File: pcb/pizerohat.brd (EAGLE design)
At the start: 65 x 29.9 mm, 21 parts, among them J1 MF-CON-2.54mm-01x03, J2 MF-CON-2.54mm-01x06, J3 MF-CON-2.54mm-01x03, J4 MF-CON-2.54mm-01x06, J5 MF-CON-2.54mm-01x03, J6 MF-CON-2.54mm-01x03, U1 MAX14778ETP+, U2 MAX3089CSD+, U3 MF-DSC-SOT233-BSS84

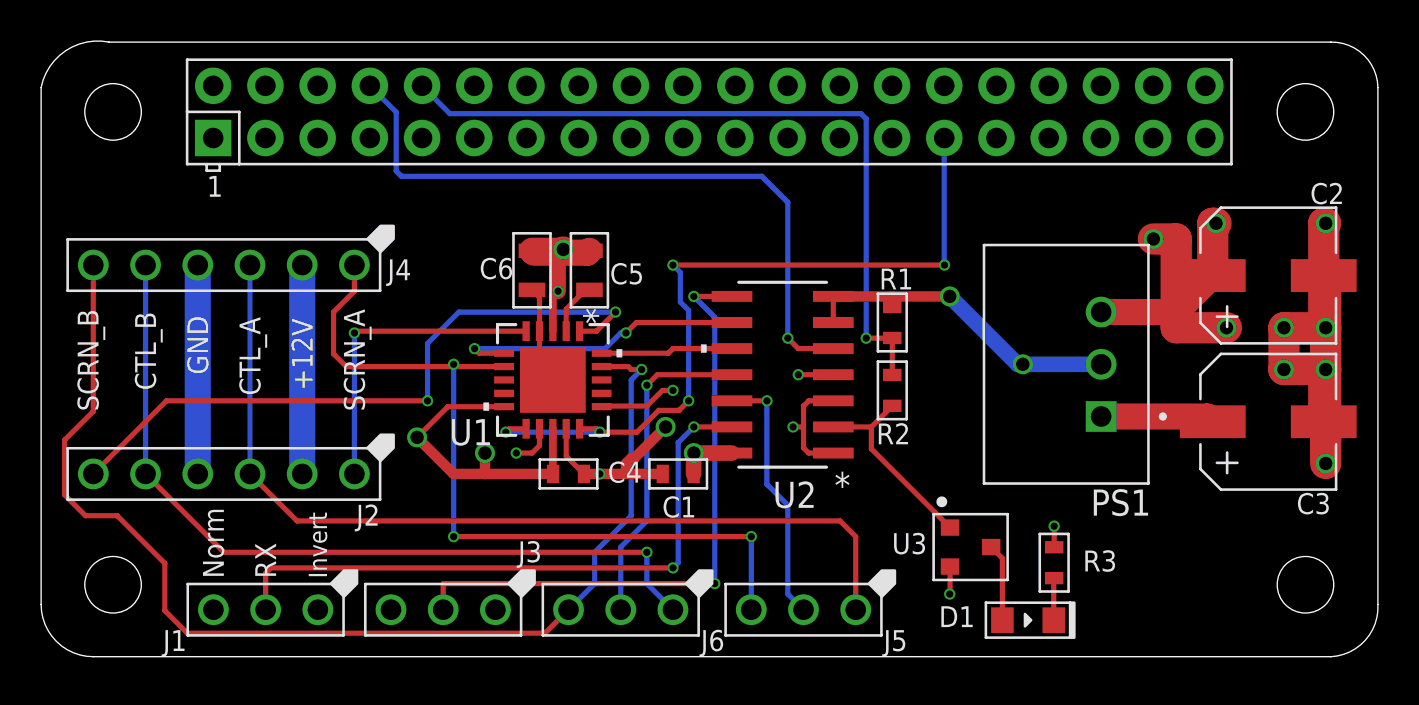
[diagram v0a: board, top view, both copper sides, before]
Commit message: Rordered mux pins, added pulldown for default muxsel
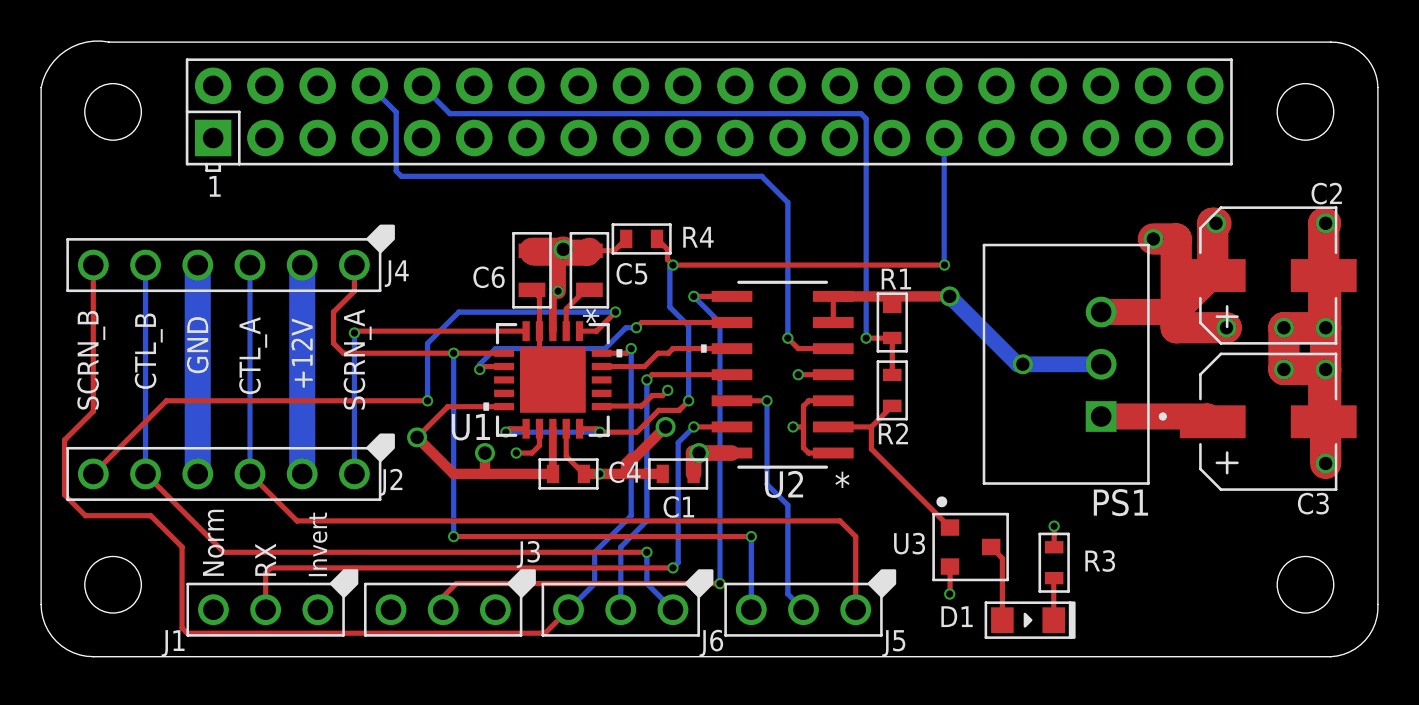
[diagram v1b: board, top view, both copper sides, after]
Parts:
- added R4: 18k, MF_Passives:R0603
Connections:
- net N$2 renamed TX_FROM_RASP
- removed net N$8: U$1.29, U1.11, U1.15
- new net MUX_SEL: R4.P$2, U$1.29, U1.11, U1.15
- net FROM_RASP_A: now also U1.7; no longer U1.6
- net FROM_RASP_B: now also U1.19; no longer U1.20
- net FROM_SCRN_A: now also U1.6; no longer U1.7
- net FROM_SCRN_B: now also U1.20; no longer U1.19
- net GND: now also R4.P$1
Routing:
- net MUX_SEL: track 0.00 -> 39.7 mm, vias 0 -> 5
- net N$8: track 37.9 -> 0.00 mm, vias 5 -> 0
- net GND: track 76.0 -> 78.0 mm
- net FROM_SCRN_B: track 56.0 -> 57.3 mm

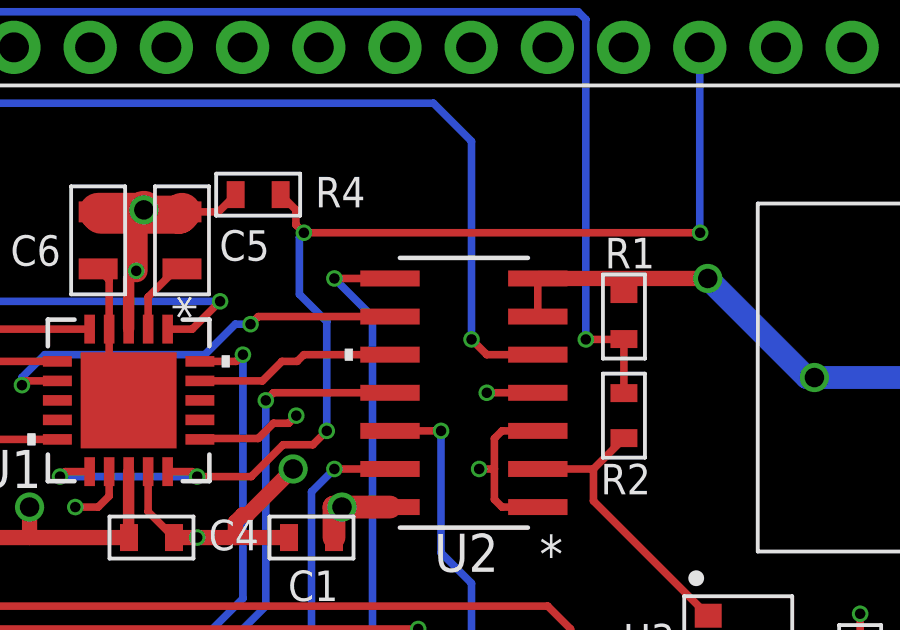
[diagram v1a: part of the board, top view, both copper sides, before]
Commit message: Power TX down when not in use
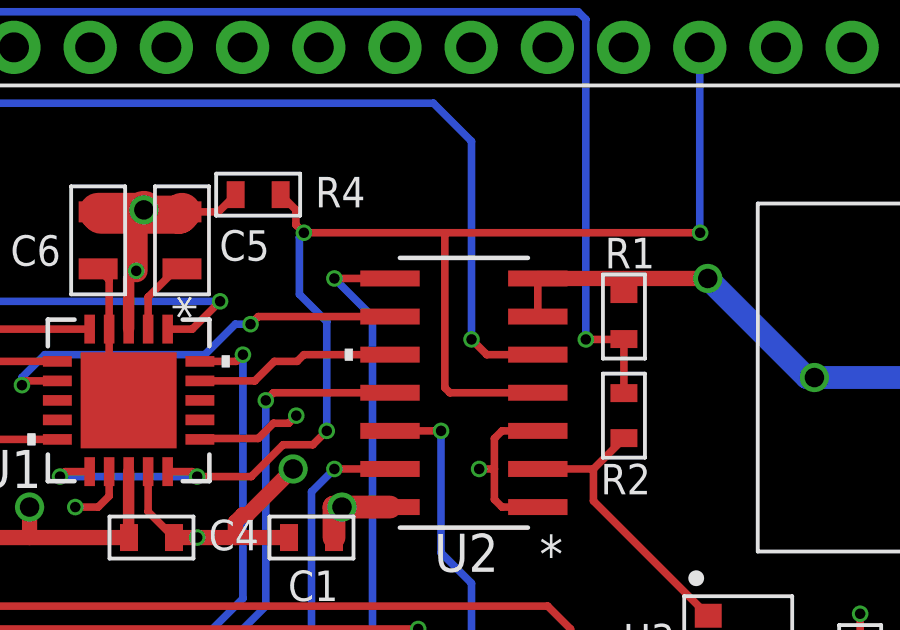
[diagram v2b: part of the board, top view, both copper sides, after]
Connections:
- net +5V: no longer U2.4
- net MUX_SEL: now also U2.4
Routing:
- net MUX_SEL: track 39.7 -> 48.0 mm
- net +5V: track 41.6 -> 39.9 mm, vias 9 -> 8
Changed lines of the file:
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@@
 <setting verticaltext="up"/>
 </settings>
-<grid distance="10" unitdist="mil" unit="mil" style="lines" multiple="1" display="no" altdistance="5" altunitdist="mil" altunit="mil"/>
+<grid distance="5" unitdist="mil" unit="mil" style="lines" multiple="1" display="no" altdistance="5" altunitdist="mil" altunit="mil"/>
 <layers>
 <layer number="1" name="Top" color="4" fill="1" visible="yes" active="yes"/>
@@
 <contactref element="U$1" pad="4"/>
 <contactref element="U$1" pad="2"/>
-<contactref element="U2" pad="14"/>
 <contactref element="J3" pad="P$1"/>
 <contactref element="J1" pad="P$1"/>
 <contactref element="C2" pad="P$1"/>
-<contactref element="C1" pad="P$1"/>
 <contactref element="C4" pad="P$1"/>
 <contactref element="U1" pad="16"/>
@@
 <wire x1="31.4071" y1="12.162" x2="28.672" y2="12.162" width="0.254" layer="1"/>
 <wire x1="28.672" y1="12.162" x2="27.178" y2="10.668" width="0.254" layer="1"/>
-<contactref element="U2" pad="4"/>
-<wire x1="47.4218" y1="13.716" x2="45.72" y2="13.716" width="0.254" layer="1"/>
 <wire x1="36.1569" y1="12.162" x2="36.1869" y2="12.192" width="0.254" layer="1"/>
 <wire x1="38.1" y1="12.192" x2="38.608" y2="12.7" width="0.254" layer="1"/>
@@
 <vertex x="9.144" y="-0.254"/>
 </polygon>
-<via x="45.72" y="13.716" extent="1-16" drill="0.35"/>
-<wire x1="42.4942" y1="9.906" x2="40.894" y2="9.906" width="0.762" layer="1"/>
-<via x="40.894" y="9.906" extent="1-16" drill="0.65"/>
-<wire x1="40.628" y1="9.906" x2="40.894" y2="9.906" width="0.762" layer="1"/>
 <wire x1="65.88" y1="18.542" x2="65.88" y2="21.082" width="1.524" layer="1"/>
 <wire x1="65.88" y1="21.082" x2="66.04" y2="21.082" width="1.524" layer="1"/>
@@
 <wire x1="53.102" y1="3.064" x2="53.086" y2="3.048" width="0.254" layer="1"/>
 <via x="53.086" y="3.048" extent="1-16" drill="0.35"/>
+<contactref element="U2" pad="14"/>
+<contactref element="C1" pad="P$1"/>
+<wire x1="42.4942" y1="9.906" x2="40.894" y2="9.906" width="0.762" layer="1"/>
+<via x="40.894" y="9.906" extent="1-16" drill="0.65"/>
+<wire x1="40.628" y1="9.906" x2="40.894" y2="9.906" width="0.762" layer="1"/>
 <wire x1="40.628" y1="8.89" x2="40.628" y2="9.906" width="0.762" layer="1"/>
 </signal>
@@
 <wire x1="34.432" y1="16.906" x2="35.372" y2="17.846" width="0.254" layer="1"/>
 </signal>
+<signal name="FROM_RASP_A">
+<contactref element="U2" pad="9"/>
+<wire x1="30.988" y1="14.986" x2="36.322" y2="14.986" width="0.254" layer="16"/>
+<wire x1="37.338" y1="16.002" x2="36.322" y2="14.986" width="0.254" layer="16"/>
+<wire x1="37.338" y1="16.002" x2="37.846" y2="16.002" width="0.254" layer="16"/>
+<via x="37.846" y="16.002" extent="1-16" drill="0.35"/>
+<wire x1="38.1" y1="16.256" x2="37.846" y2="16.002" width="0.254" layer="1"/>
+<wire x1="42.4942" y1="16.256" x2="38.1" y2="16.256" width="0.254" layer="1"/>
+<contactref element="U1" pad="7"/>
+<wire x1="31.4071" y1="14.112" x2="30.368" y2="14.112" width="0.254" layer="1"/>
+<wire x1="30.368" y1="14.112" x2="30.226" y2="13.97" width="0.254" layer="1"/>
+<via x="30.226" y="13.97" extent="1-16" drill="0.35"/>
+<wire x1="30.226" y1="13.97" x2="30.226" y2="14.224" width="0.254" layer="16"/>
+<wire x1="30.226" y1="14.224" x2="30.988" y2="14.986" width="0.254" layer="16"/>
+</signal>
+<signal name="FROM_RASP_B">
+<contactref element="U2" pad="10"/>
+<wire x1="39.4" y1="14.762" x2="39.624" y2="14.986" width="0.254" layer="1"/>
+<wire x1="39.624" y1="14.986" x2="42.4942" y2="14.986" width="0.254" layer="1"/>
+<contactref element="U1" pad="19"/>
+<wire x1="36.1569" y1="14.112" x2="37.988" y2="14.112" width="0.254" layer="1"/>
+<wire x1="38.638" y1="14.762" x2="39.4" y2="14.762" width="0.254" layer="1"/>
+<wire x1="37.988" y1="14.112" x2="38.638" y2="14.762" width="0.254" layer="1"/>
+</signal>
+<signal name="N$6">
+<contactref element="R3" pad="P$2"/>
+<contactref element="D1" pad="CATHODE"/>
+<wire x1="58.146" y1="1.778" x2="58.146" y2="3.802" width="0.254" layer="1"/>
+<wire x1="58.146" y1="3.802" x2="58.166" y2="3.822" width="0.254" layer="1"/>
+</signal>
+<signal name="N$9">
+<contactref element="D1" pad="ANODE"/>
+<contactref element="U3" pad="P$3"/>
+<wire x1="55.102" y1="5.334" x2="55.646" y2="4.79" width="0.254" layer="1"/>
+<wire x1="55.646" y1="4.79" x2="55.646" y2="1.778" width="0.254" layer="1"/>
+</signal>
 <signal name="MUX_SEL">
+<contactref element="U2" pad="4"/>
 <contactref element="U1" pad="15"/>
 <contactref element="U1" pad="11"/>
 <contactref element="U$1" pad="29"/>
+<contactref element="R4" pad="P$2"/>
 <wire x1="32.482" y1="11.0871" x2="31.6611" y2="11.0871" width="0.254" layer="1"/>
 <wire x1="31.6611" y1="11.0871" x2="31.496" y2="10.922" width="0.254" layer="1"/>
@@
 <wire x1="52.82" y1="19.062" x2="52.832" y2="19.05" width="0.254" layer="16"/>
 <via x="52.832" y="19.05" extent="1-16" drill="0.35"/>
-<wire x1="52.832" y1="19.05" x2="39.624" y2="19.05" width="0.254" layer="1"/>
+<wire x1="52.832" y1="19.05" x2="44.323" y2="19.05" width="0.254" layer="1"/>
 <via x="39.624" y="19.05" extent="1-16" drill="0.35"/>
+<wire x1="44.323" y1="19.05" x2="39.624" y2="19.05" width="0.254" layer="1"/>
 <wire x1="35.082" y1="11.0871" x2="35.9029" y2="11.0871" width="0.254" layer="1"/>
 <wire x1="35.9029" y1="11.0871" x2="36.068" y2="10.922" width="0.254" layer="1"/>
@@
 <wire x1="40.386" y1="12.446" x2="40.386" y2="16.0880125" width="0.254" layer="16"/>
 <wire x1="39.358" y1="19.316" x2="39.624" y2="19.05" width="0.254" layer="1"/>
-<contactref element="R4" pad="P$2"/>
 <wire x1="38.85" y1="20.32" x2="39.358" y2="19.812" width="0.254" layer="1"/>
 <wire x1="39.358" y1="19.812" x2="39.358" y2="19.316" width="0.254" layer="1"/>
-</signal>
-<signal name="FROM_RASP_A">
-<contactref element="U2" pad="9"/>
-<wire x1="30.988" y1="14.986" x2="36.322" y2="14.986" width="0.254" layer="16"/>
-<wire x1="37.338" y1="16.002" x2="36.322" y2="14.986" width="0.254" layer="16"/>
-<wire x1="37.338" y1="16.002" x2="37.846" y2="16.002" width="0.254" layer="16"/>
-<via x="37.846" y="16.002" extent="1-16" drill="0.35"/>
-<wire x1="38.1" y1="16.256" x2="37.846" y2="16.002" width="0.254" layer="1"/>
-<wire x1="42.4942" y1="16.256" x2="38.1" y2="16.256" width="0.254" layer="1"/>
-<contactref element="U1" pad="7"/>
-<wire x1="31.4071" y1="14.112" x2="30.368" y2="14.112" width="0.254" layer="1"/>
-<wire x1="30.368" y1="14.112" x2="30.226" y2="13.97" width="0.254" layer="1"/>
-<via x="30.226" y="13.97" extent="1-16" drill="0.35"/>
-<wire x1="30.226" y1="13.97" x2="30.226" y2="14.224" width="0.254" layer="16"/>
-<wire x1="30.226" y1="14.224" x2="30.988" y2="14.986" width="0.254" layer="16"/>
-</signal>
-<signal name="FROM_RASP_B">
-<contactref element="U2" pad="10"/>
-<wire x1="39.4" y1="14.762" x2="39.624" y2="14.986" width="0.254" layer="1"/>
-<wire x1="39.624" y1="14.986" x2="42.4942" y2="14.986" width="0.254" layer="1"/>
-<contactref element="U1" pad="19"/>
-<wire x1="36.1569" y1="14.112" x2="38.242" y2="14.112" width="0.254" layer="1"/>
-<wire x1="38.892" y1="14.762" x2="39.4" y2="14.762" width="0.254" layer="1"/>
-<wire x1="38.242" y1="14.112" x2="38.892" y2="14.762" width="0.254" layer="1"/>
-</signal>
-<signal name="N$6">
-<contactref element="R3" pad="P$2"/>
-<contactref element="D1" pad="CATHODE"/>
-<wire x1="58.146" y1="1.778" x2="58.146" y2="3.802" width="0.254" layer="1"/>
-<wire x1="58.146" y1="3.802" x2="58.166" y2="3.822" width="0.254" layer="1"/>
-</signal>
-<signal name="N$9">
-<contactref element="D1" pad="ANODE"/>
-<contactref element="U3" pad="P$3"/>
-<wire x1="55.102" y1="5.334" x2="55.646" y2="4.79" width="0.254" layer="1"/>
-<wire x1="55.646" y1="4.79" x2="55.646" y2="1.778" width="0.254" layer="1"/>
+<wire x1="47.4218" y1="13.716" x2="44.4917125" y2="13.716" width="0.254" layer="1"/>
+<wire x1="44.4917125" y1="13.716" x2="44.323" y2="13.8847125" width="0.254" layer="1"/>
+<wire x1="44.323" y1="13.8847125" x2="44.323" y2="19.05" width="0.254" layer="1"/>
 </signal>
 </signals>
